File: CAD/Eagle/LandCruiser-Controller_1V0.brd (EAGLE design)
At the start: 99 x 64.8 mm, 56 parts, among them K311 V23086C1001A403, K312 V23086C1001A403, K313 V23086C1001A403, K314 V23086C1001A403, K315 V23086C1001A403, U101 MEGA8-P, U221 SN75240, U301 MIC2981/2982SO18W, U501 MAX232_SOIC16, U611 LM7805, X201 WEIDMUELLER 1234600000, X321 WEIDMUELLER 1234600000, X401 I2C

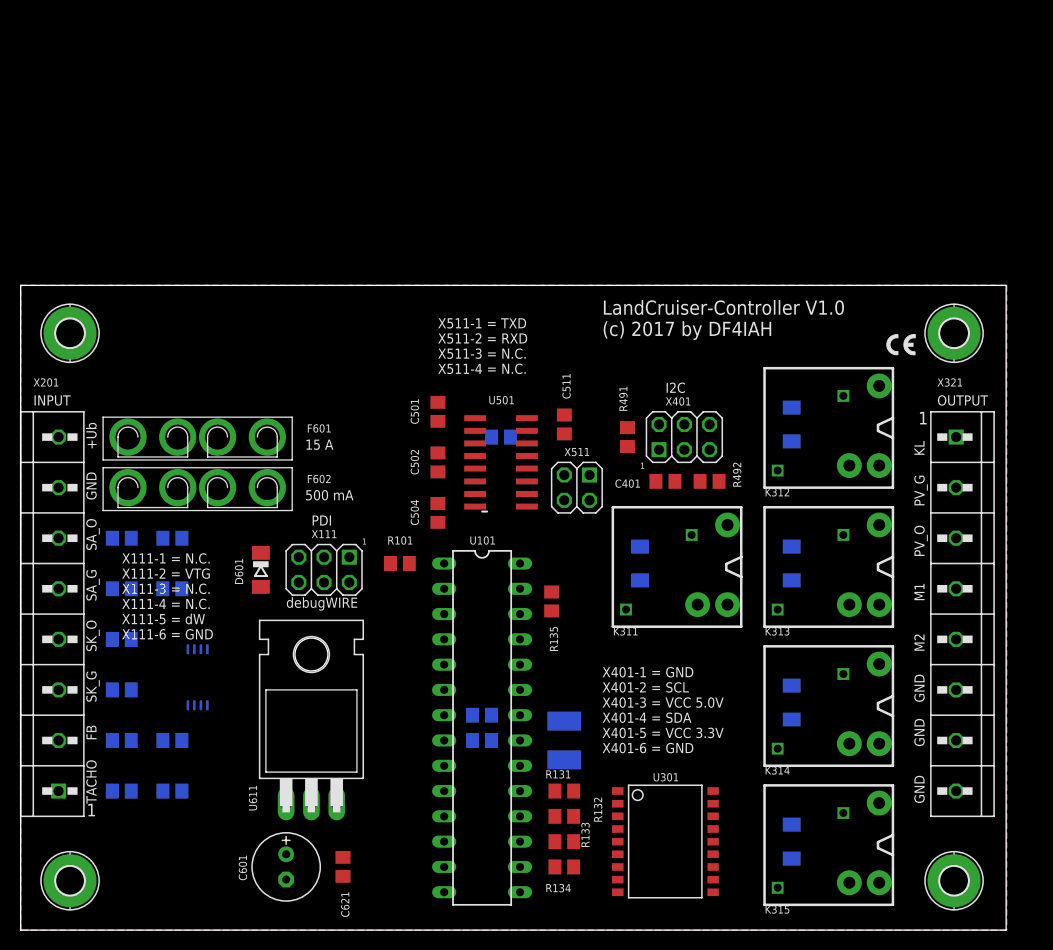
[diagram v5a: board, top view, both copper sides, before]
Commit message: HW_V1.0 - Place&Routing - placement done, half of the routing done
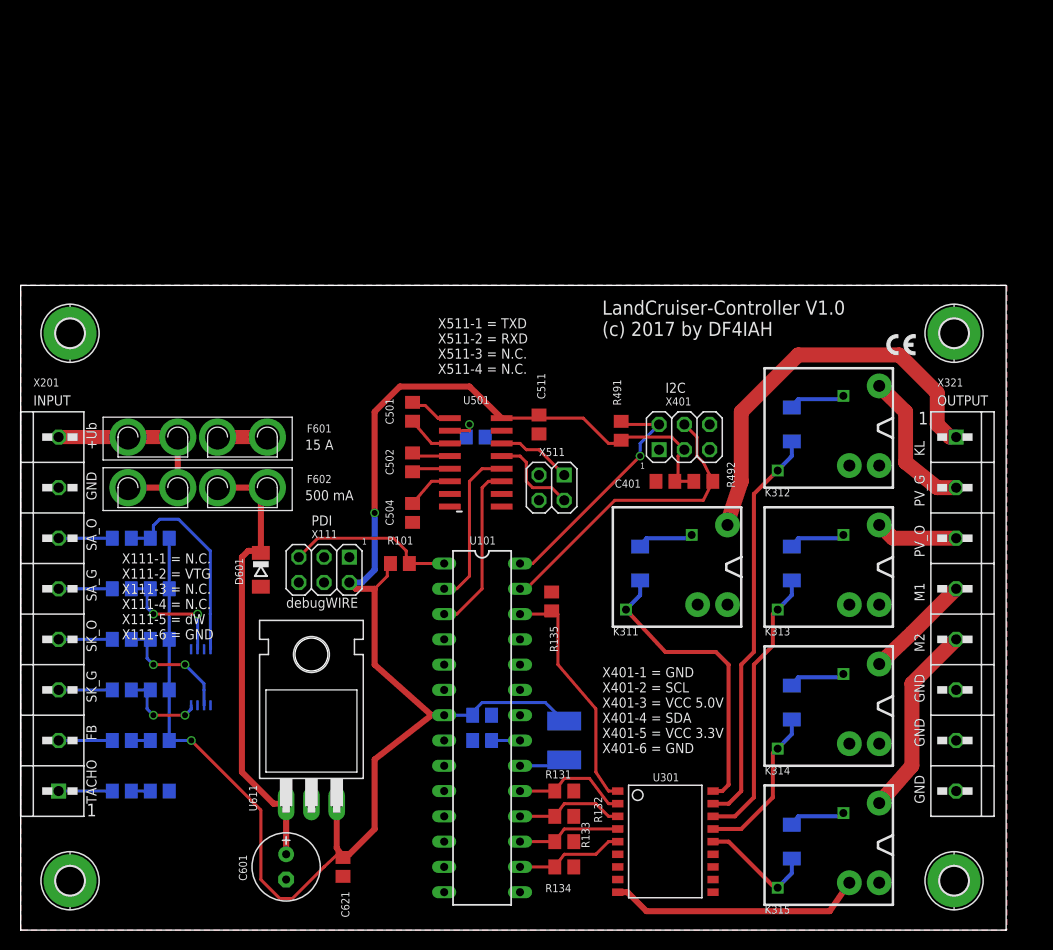
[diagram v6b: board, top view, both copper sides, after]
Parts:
- removed R121: 4k7R, rcl:R0805
- removed R232: 22kR, rcl:R0805
- added R124, R125, R126: 4k7R, rcl:R0805
- added R216: 56R, rcl:R0805
- R211: value 56R -> 22kR
- moved R122 15.3 mm to (14.0, 19.1)
- moved R123 5.24 mm to (14.0, 24.1), turned to 0 degrees
- moved R213 5.08 mm to (10.2, 24.1)
- moved R211 5.08 mm to (10.2, 14.0), turned to 0 degrees
- moved R212 5.08 mm to (10.2, 19.1)
- moved R214 5.08 mm to (10.2, 29.2)
- moved R215 5.08 mm to (10.2, 34.3)
- moved C501 2.54 mm to (39.4, 52.1)
- moved C502 2.54 mm to (39.4, 47.0)
- moved C503 2.54 mm to (45.7, 49.5)
- moved C504 2.54 mm to (39.4, 41.9)
- moved C511 2.54 mm to (52.1, 50.8)
- moved U501 2.54 mm to (45.7, 47.0)
- moved X511 2.54 mm to (53.3, 44.5)
- moved R231 1.27 mm to (14.0, 14.0)
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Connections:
- net +12V: now also F601.3, F601.4; no longer F601.P$3, F601.P$4
- net +5V: now also R123.1, R124.1, R125.2, R126.2; no longer R121.2, R123.2
- net +UB: now also F601.1, F601.2, F602.1, F602.2; no longer F601.P$1, F601.P$2, F602.P$1, F602.P$2
- net ECU_FB: now also R212.1; no longer R211.1
- net MP_FB: now also R122.1, R212.2; no longer R123.1, R211.2
- net MP_SA_G: now also R125.1, R215.2; no longer R122.1, R214.2
- net MP_SA_O: now also R126.1, R216.2; no longer R121.1, R215.2
- net MP_SK_G: now also R123.2, R213.2; no longer R212.2
- net MP_SK_O: now also R124.2, R214.2; no longer R213.2
- net MP_TACHO: now also R211.1; no longer R232.1
- net REGIN: now also F602.3, F602.4; no longer F602.P$3, F602.P$4
- net SA_G: now also R215.1; no longer R214.1
- net SA_O: now also R216.1; no longer R215.1
- net SK_G: now also R213.1; no longer R212.1
- net SK_O: now also R214.1; no longer R213.1
- net TACHO: now also R211.2; no longer R232.2
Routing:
- net +5V: track 0.00 -> 170.0 mm, vias 0 -> 2
- net +12V: track 0.00 -> 59.8 mm
- net REGIN: track 0.00 -> 46.3 mm
- net KL: track 0.00 -> 40.8 mm
- net DRV_PV_G: track 0.00 -> 40.6 mm
- net SDA: track 0.00 -> 31.0 mm
- net DRV_KL: track 0.00 -> 30.1 mm
- net DRV_PV_O: track 0.00 -> 28.3 mm
- net MP_KL: track 0.00 -> 24.5 mm
- net SCL: track 0.00 -> 24.4 mm, vias 0 -> 1
- net +UB: track 0.00 -> 22.0 mm
- net MP_SA_O: track 0.00 -> 20.4 mm
- net M2: track 0.00 -> 19.5 mm
- net MP_TXD: track 0.00 -> 17.3 mm
- net !RST: track 0.00 -> 16.9 mm
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
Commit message: HW_V1.0 - Routing - routing finished, no ground polygone here
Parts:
- moved R134 3.81 mm to (54.6, 2.54)
- moved R133 2.54 mm to (54.6, 6.35)
- moved C511 1.27 mm to (53.3, 50.8)
- moved R132 1.27 mm to (54.6, 10.2)
- moved R492 0.90 mm to (67.9, 44.5)
- moved C401 0.90 mm to (64.1, 44.5)
- moved C101 0.64 mm to (46.4, 21.0)
- moved C102 0.64 mm to (46.4, 18.4)
- moved D601 0.64 mm to (24.8, 36.2)
- moved L101 0.63 mm to (54.6, 19.7)
- moved X511 0.63 mm to (54.0, 44.5)
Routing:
- net +12V: track 59.8 -> 170.4 mm
- net MP_TACHO: track 1.91 -> 71.2 mm, vias 0 -> 1
- net MP_SA_G: track 12.8 -> 49.6 mm, vias 2 -> 4
- net MP_SA_O: track 20.4 -> 57.0 mm, vias 0 -> 2
- net MP_FB: track 1.91 -> 36.0 mm
- net MP_SK_G: track 9.22 -> 41.9 mm, vias 2 -> 4
- net MP_SK_O: track 12.8 -> 43.8 mm, vias 2 -> 4
- net SDA: track 31.0 -> 38.1 mm
- net MP_M2: track 11.0 -> 16.3 mm
- net RXD: track 9.25 -> 13.3 mm
- net MP_M1: track 10.5 -> 13.2 mm
- net +5V: track 170.0 -> 171.3 mm
- net MP_PV_G: track 11.7 -> 12.9 mm
- net REGIN: track 46.3 -> 47.4 mm
- net MP_PV_O: track 11.0 -> 12.0 mm
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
